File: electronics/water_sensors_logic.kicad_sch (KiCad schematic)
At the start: 0 parts

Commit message: lisbon flight changes
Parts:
- added J10: water_sensor_conn, TerminalBlock:TerminalBlock_Xinya_XY308-2.54-6P_1x06_P2.54mm_Horizontal, symbol Connector_Generic:Conn_01x06
- added Q1: BF245B, Package_TO_SOT_THT:TO-92_Inline, symbol Transistor_FET:BF245B
- added R17: 4.7k, symbol Device:R
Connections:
- new net +3.3V: Q1.3 (D)
- new net GND_LP: R17.2
- new net WS_ENABLE: Q1.1 (G), R17.1
- new net ws_rod_0: J10.1 (Pin_1), Q1.2 (S)
- new net ws_rod_1: J10.2 (Pin_2)
- new net ws_rod_2: J10.3 (Pin_3)
- new net ws_rod_3: J10.4 (Pin_4)
- new net ws_rod_4: J10.5 (Pin_5)
- new net ws_rod_5: J10.6 (Pin_6)
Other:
- added sheet WS_option_1 (option_1.kicad_sch)
- added sheet WS_option_2 (option_2.kicad_sch)
- note added: "WS option 2 - 6 wires from sensor and all logic on CCU"

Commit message: flight back. different layout. start analog ui
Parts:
- removed J10: water_sensor_conn, TerminalBlock:TerminalBlock_Xinya_XY308-2.54-6P_1x06_P2.54mm_Horizontal, symbol Connector_Generic:Conn_01x06
- removed Q1: BF245B, Package_TO_SOT_THT:TO-92_Inline, symbol Transistor_FET:BF245B
- added J16: Conn_01x02, TerminalBlock:TerminalBlock_Xinya_XY308-2.54-2P_1x02_P2.54mm_Horizontal, symbol Connector_Generic:Conn_01x02
- added J20: water_sensor_conn, TerminalBlock:TerminalBlock_Xinya_XY308-2.54-5P_1x05_P2.54mm_Horizontal, symbol Connector_Generic:Conn_01x05
- added Q1: Q_PMOS_GDS, Package_TO_SOT_SMD:SOT-23_Handsoldering, symbol Device:Q_PMOS_GDS
- added R26, R28, R29, R30, R31, R32: 4.7k, Resistor_SMD:R_0805_2012Metric_Pad1.20x1.40mm_HandSolder, symbol Device:R
- added U16: ULN2003, Package_SO:SO-16_3.9x9.9mm_P1.27mm, symbol Transistor_Array:ULN2003
- R17: value 4.7k -> 1k; footprint (none) -> Resistor_SMD:R_0805_2012Metric_Pad1.20x1.40mm_HandSolder
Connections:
- net +3.3V: now also Q1.2 (D), R26.1, R28.1, R29.1, R30.1, R31.1, R32.1
- net GND_LP: now also U16.8 (GND); no longer R17.2
- net WS_ENABLE: now also R26.2
- net ws_rod_0: now also J16.1 (Pin_1), J20.1 (Pin_1), Q1.3 (S)
- net ws_rod_1: now also J20.2 (Pin_2), U16.5 (I5)
- net ws_rod_2: now also J20.3 (Pin_3), U16.4 (I4)
- net ws_rod_3: now also J20.4 (Pin_4), U16.3 (I3)
- net ws_rod_4: now also J20.5 (Pin_5), U16.2 (I2)
- new net: Q1.1 (G), R17.2
- new net GREY_WATER_FULL: R28.2, U16.16 (O1)
- new net WS_LVL_100%: R29.2, U16.15 (O2)
- new net WS_LVL_25%: R32.2, U16.12 (O5)
- new net WS_LVL_50%: R31.2, U16.13 (O4)
- new net WS_LVL_75%: R30.2, U16.14 (O3)
- new net grey_water_rod: J16.2 (Pin_2), U16.1 (I1)
- no-connect marks 0 -> 5
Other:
- removed sheet WS_option_1
- note added: "PULL-DOWN to enable"
- note removed: "WS option 2 - 6 wires from sensor and all logic on CCU"
- moved on the sheet: R17

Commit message: no tracks, but placement looks good
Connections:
- no-connect marks 5 -> 8
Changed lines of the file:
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@@
+	)
+	(no_connect
+		(at 167.64 138.43)
 	)
 	(no_connect
@@
 		(at 196.85 68.58)
 	)
+	(no_connect
+		(at 167.64 143.51)
+	)
+	(no_connect
+		(at 167.64 140.97)
+	)
 	(bus_entry

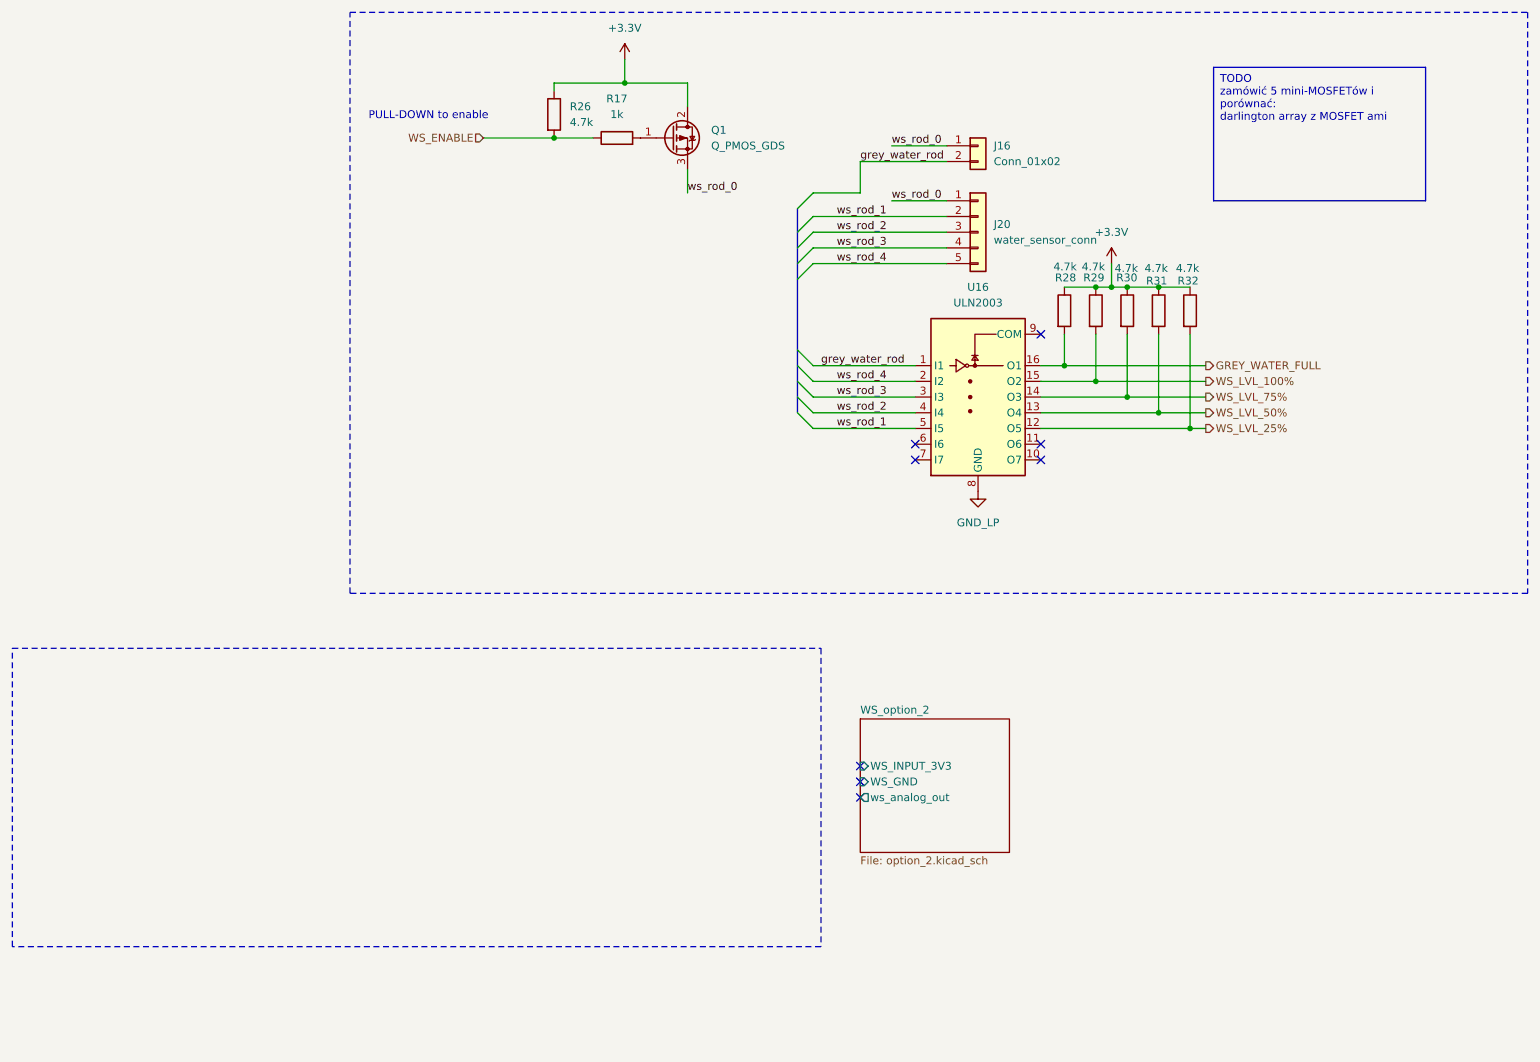
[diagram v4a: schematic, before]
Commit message: start to create BOM and finalising symbol fields
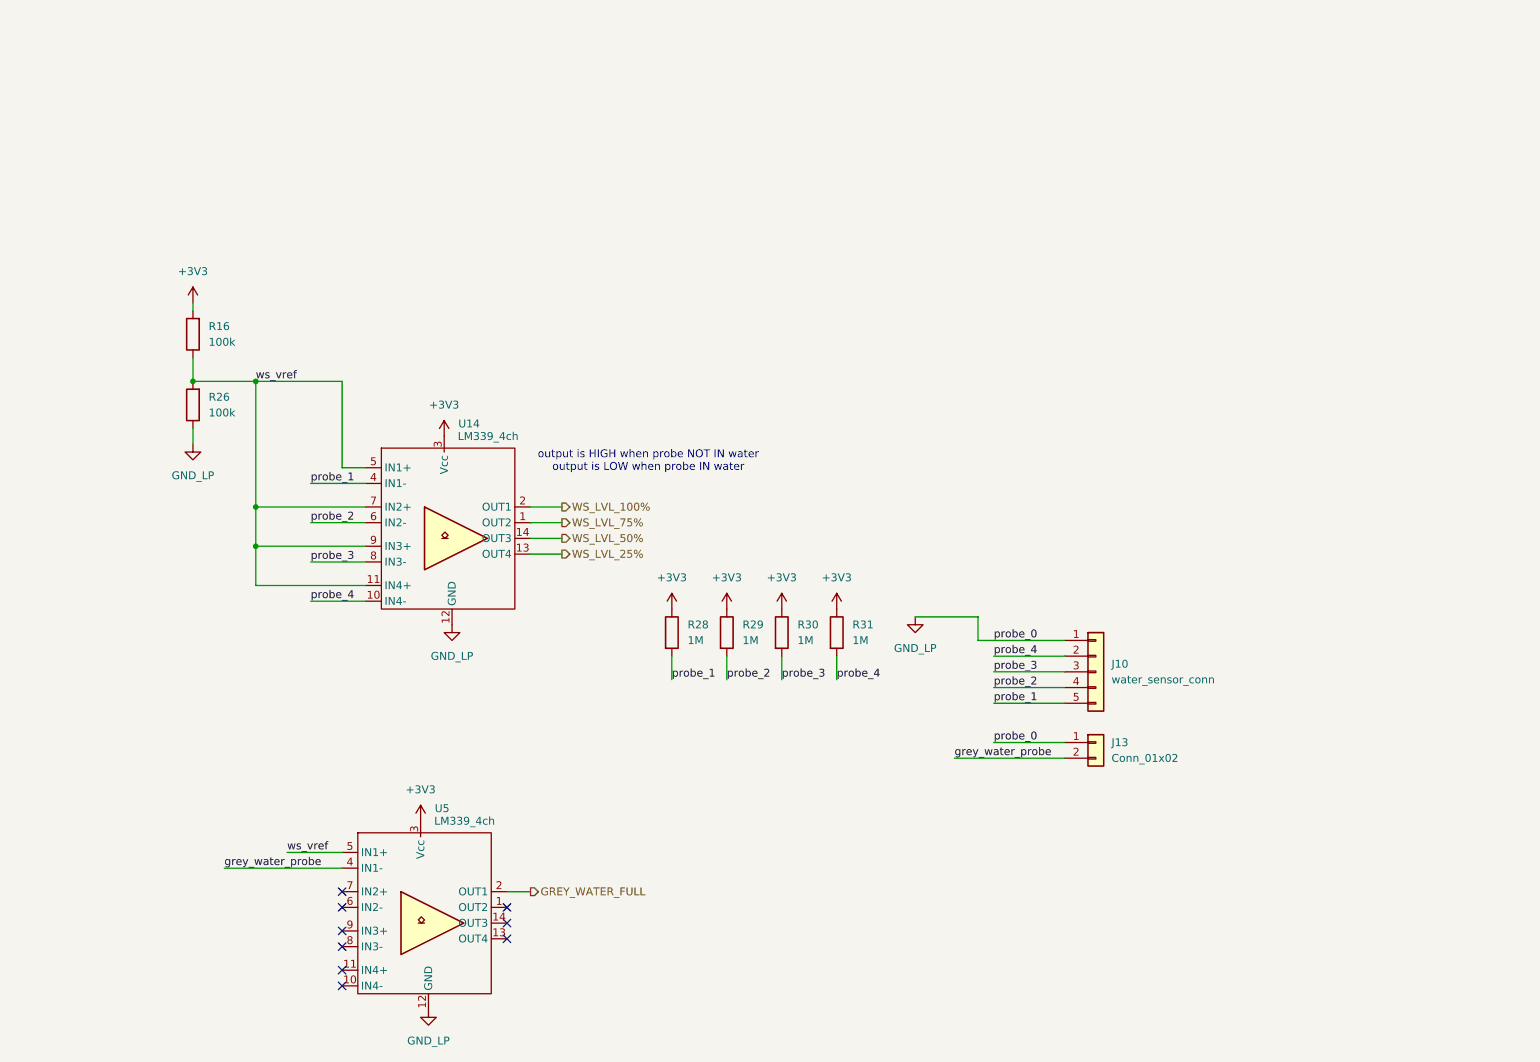
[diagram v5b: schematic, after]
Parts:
- removed J16: Conn_01x02, TerminalBlock:TerminalBlock_Xinya_XY308-2.54-2P_1x02_P2.54mm_Horizontal, symbol Connector_Generic:Conn_01x02
- removed J20: water_sensor_conn, TerminalBlock:TerminalBlock_Xinya_XY308-2.54-5P_1x05_P2.54mm_Horizontal, symbol Connector_Generic:Conn_01x05
- removed Q1: Q_PMOS_GDS, Package_TO_SOT_SMD:SOT-23_Handsoldering, symbol Device:Q_PMOS_GDS
- removed R17: 1k, Resistor_SMD:R_0805_2012Metric_Pad1.20x1.40mm_HandSolder, symbol Device:R
- removed R32: 4.7k, Resistor_SMD:R_0805_2012Metric_Pad1.20x1.40mm_HandSolder, symbol Device:R
- removed U16: ULN2003, Package_SO:SO-16_3.9x9.9mm_P1.27mm, symbol Transistor_Array:ULN2003
- added J10: water_sensor_conn, TerminalBlock:TerminalBlock_Xinya_XY308-2.54-5P_1x05_P2.54mm_Horizontal, symbol Connector_Generic:Conn_01x05
- added J13: Conn_01x02, TerminalBlock:TerminalBlock_Xinya_XY308-2.54-2P_1x02_P2.54mm_Horizontal, symbol Connector_Generic:Conn_01x02
- added R16: 100k, Resistor_SMD:R_0805_2012Metric, symbol Device:R
- added U14, U5: LM339_4ch, Package_SO:SOIC-14_3.9x8.7mm_P1.27mm, symbol HeavyDuty:LM339_4ch
- R26: value 4.7k -> 100k; footprint Resistor_SMD:R_0805_2012Metric_Pad1.20x1.40mm_HandSolder -> Resistor_SMD:R_0805_2012Metric
- R28, R29, R30, R31: value 4.7k -> 1M; footprint Resistor_SMD:R_0805_2012Metric_Pad1.20x1.40mm_HandSolder -> Resistor_SMD:R_0805_2012Metric
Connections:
- net GND_LP: now also R26.1, J10.1 (Pin_1), J13.1 (Pin_1), U14.12 (GND), U5.12 (GND)
- net GREY_WATER_FULL: now also U5.2 (OUT1); no longer R28.2
- net WS_LVL_100%: now also U14.2 (OUT1); no longer R29.2
- net WS_LVL_25%: now also U14.13 (OUT4)
- net WS_LVL_50%: now also U14.14 (OUT3); no longer R31.2
- net WS_LVL_75%: now also U14.1 (OUT2); no longer R30.2
- net +3.3V renamed +3V3
- net +3V3: now also R16.2, U14.3 (Vcc), U5.3 (Vcc); no longer R26.1
- net WS_ENABLE renamed ws_vref
- net ws_vref: now also R16.1, U14.11 (IN4+), U14.5 (IN1+), U14.7 (IN2+), U14.9 (IN3+), U5.5 (IN1+)
- new net grey_water_probe: J13.2 (Pin_2), U5.4 (IN1-)
- new net probe_1: J10.5 (Pin_5), R28.2, U14.4 (IN1-)
- new net probe_2: J10.4 (Pin_4), R29.2, U14.6 (IN2-)
- new net probe_3: J10.3 (Pin_3), R30.2, U14.8 (IN3-)
- new net probe_4: J10.2 (Pin_2), R31.2, U14.10 (IN4-)
- no-connect marks 8 -> 9
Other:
- removed sheet WS_option_2
- note added: "output is HIGH when probe NOT IN water output is LOW when probe IN water"
- note removed: "PULL-DOWN to enable"
